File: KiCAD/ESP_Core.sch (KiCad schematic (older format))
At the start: 8 parts, among them J201 Conn_02x04_Counter_Clockwise, U201 ESP32-PICO-D4

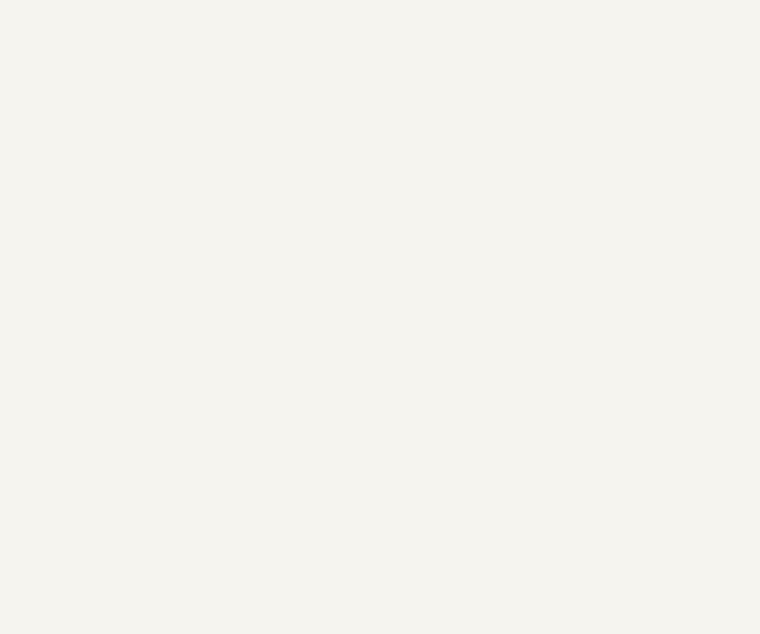
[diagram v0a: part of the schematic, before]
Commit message: Continue work on Schematics
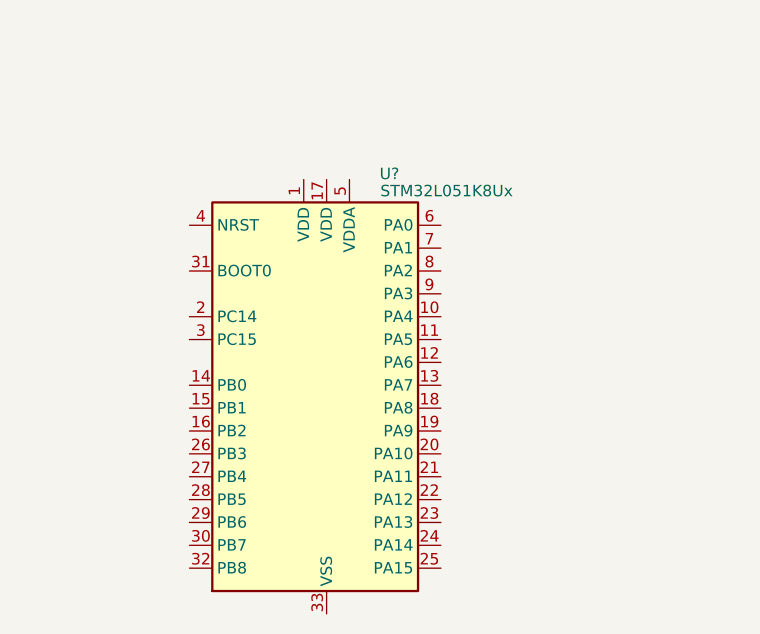
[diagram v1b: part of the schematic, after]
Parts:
- added U?: STM32L051K8Ux, Package_DFN_QFN:QFN-32-1EP_5x5mm_P0.5mm_EP3.45x3.45mm, symbol MCU_ST_STM32L0:STM32L051K8Ux
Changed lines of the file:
@@
 $Descr A4 11693 8268
 encoding utf-8
-Sheet 2 6
+Sheet 2 7
 Title ""
 Date ""
@@
 Text Label 7625 4225 0    50   ~ 0
 STATE_LED
+$Comp
+L MCU_ST_STM32L0:STM32L051K8Ux U?
+U 1 1 6106CA64
+P 2500 5100
+F 0 "U?" H 2775 6025 50  0000 C CNN
+F 1 "STM32L051K8Ux" H 3025 5950 50  0000 C CNN
+F 2 "Package_DFN_QFN:QFN-32-1EP_5x5mm_P0.5mm_EP3.45x3.45mm" H 2000 4200 50  0001 R CNN
+F 3 "http://www.st.com/st-web-ui/static/active/en/resource/technical/document/datasheet/DM00108219.pdf" H 2500 5100 50  0001 C CNN
+	1    2500 5100
+	1    0    0    -1
+$EndComp
 $EndSCHEMATC

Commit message: Add STM32 base circuit for power control and USB, also a lot of other things
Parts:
- removed U?: STM32L051K8Ux, Package_DFN_QFN:QFN-32-1EP_5x5mm_P0.5mm_EP3.45x3.45mm, symbol MCU_ST_STM32L0:STM32L051K8Ux
- added C204: 1uF 0402, Capacitor_SMD:C_0402_1005Metric, symbol Device:C_Small
- added C205: 0.1uF 0402, Capacitor_SMD:C_0402_1005Metric, symbol Device:C_Small
- added PW201: AP7354-33FS4, XasPrints:X2-DFN1010-4, symbol XasParts:AP7354-33FS4
- added R202: 10k 0402, Resistor_SMD:R_0402_1005Metric, symbol Device:R_Small
- added R203: 0402 100k, Resistor_SMD:R_0402_1005Metric, symbol Device:R_Small
- added R204: 0402 33k, Resistor_SMD:R_0402_1005Metric, symbol Device:R_Small
- added R205: 0402 10k, Resistor_SMD:R_0402_1005Metric, symbol Device:R_Small
- added SW201: SW_Push, Button_Switch_SMD:SW_SPST_B3U-1000P, symbol Switch:SW_Push
- added U202: STM32L052K8Ux, Package_DFN_QFN:QFN-32-1EP_5x5mm_P0.5mm_EP3.45x3.45mm, symbol MCU_ST_STM32L0:STM32L052K8Ux
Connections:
- net BOOT: now also U202.26 (PB3)
- net E>P: now also U202.20 (PA10)
- net GND: now also C204.2, C205.2, PW201.2 (GND), PW201.5 (EP), SW201.2, U202.33 (VSS)
- net P>E: now also R205.1
- net RESET: now also U202.27 (PB4)
- net SCL: now reaches U201.17 (IO14)
- net SCL: now also U202.29 (PB6)
- net SDA: now reaches U201.18 (IO12)
- net SDA: now also U202.30 (PB7)
- net AUDIO_LRCK: now reaches U201.36 (IO23)
- net AUDIO_BCK: now reaches U201.38 (IO19)
- net SPKR_DATA: now reaches U201.39 (IO22)
- net MIC_DATA: now reaches U201.42 (IO21)
- net STM_SWDIO: now reaches J201.4 (Pin_4)
- net STM_SWDIO: now also U202.23 (PA13)
- net STM_SWCLK: now reaches J201.5 (Pin_5)
- net STM_SWCLK: now also U202.24 (PA14)
- net +BATT renamed +5V
- net +5V: now also PW201.3 (EN), PW201.4 (VIN)
- new net: C204.1, C205.1, PW201.1 (OUT), R202.1, U202.17 (VDD), U202.5 (VDDA)
- new net: R203.2, R204.1, U202.7 (PA1)
- new net: R204.2, U202.8 (PA2)
- new net: R202.2, SW201.1, U202.6 (PA0)
- new net: R205.2, U202.19 (PA9)
- new net: U202.1 (VDD), U202.4 (NRST)
- new net BAT_ON: U202.3 (PC15)
- new net GLOW_ON: U202.2 (PC14)
- new net MAIN_PWR_ON: U202.18 (PA8)
- new net RAW_BAT: R203.1
- new net USB_DM: U202.21 (PA11)
- new net USB_DP: U202.22 (PA12)
- no-connect marks 13 -> 11

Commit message: Continue work on TapV2's schematic, almost completing it!
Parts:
- added R206: 10k 0402, Resistor_SMD:R_0402_1005Metric, symbol Device:R_Small
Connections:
- net GND: now also U202.31 (BOOT0)
- net STATE_LED: now also U201.14 (IO25)
- net IR_TX: now reaches U201.34 (IO5)
- net IR_RX: now reaches U201.35 (IO18)
- net STM_RST: now reaches J201.8 (Pin_8)
- net STM_RST: now also U202.4 (NRST), R206.2
- net at C204.1, C205.1, PW201.1 (OUT)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: now also U202.1 (VDD), R206.1
- net CAM_CS: now reaches U202.10 (PA4)
- net CAM_DCLK: now reaches U202.11 (PA5)
- net CAM_PILOT_CLOCK: now reaches U202.12 (PA6)
- net CAM_DATA: now reaches U202.13 (PA7)
- no-connect marks 11 -> 10
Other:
- moved on the sheet: C204, C205, PW201, R202, R203, R204, R205, SW201, U202

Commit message: Finalize PCB schematics
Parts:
- added J202: Conn_01x04_Female, Connector_PinHeader_1.27mm:PinHeader_1x04_P1.27mm_Vertical, symbol Connector:Conn_01x04_Female
- added JP201: SolderJumper_3_Bridged12, Jumper:SolderJumper-3_P1.3mm_Open_RoundedPad1.0x1.5mm, symbol Jumper:SolderJumper_3_Bridged12
- added R207: 36R 0402, Resistor_SMD:R_0402_1005Metric, symbol Device:R_Small
- added R208: 10k 0402, Resistor_SMD:R_0402_1005Metric, symbol Device:R_Small
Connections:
- net +3V3: now also J202.2 (Pin_2)
- net AUDIO_LRCK: now also U201.15 (IO26); no longer U201.36 (IO23)
- net GLOW_ON: now also JP201.2 (C); no longer U202.2 (PC14)
- net GND: now also J202.1 (Pin_1), R208.1
- net IR_RX: now also U201.16 (IO27); no longer U201.35 (IO18)
- net MIC_DATA: now also U201.18 (IO12), R208.2; no longer U201.42 (IO21)
- net SDA: now also U201.42 (IO21); no longer U201.18 (IO12)
- net KNOCK_INT: now reaches U201.12 (IO32)
- net EXT_1: now reaches U201.20 (IO13)
- net EXT_1: now also J202.3 (Pin_3)
- net EXT_2: now reaches U201.21 (IO15)
- net EXT_2: now also J202.4 (Pin_4)
- net ESP_GLOW_ON: now reaches U201.24 (IO4)
- net ESP_GLOW_ON: now also JP201.3 (B)
- net ~VUSB_PRESENT: now reaches U202.14 (PB0)
- net ~CHG: now reaches U202.16 (PB2)
- net STATE_LED: no longer names the net of U201.14 (IO25)
- net STATE_LED: now also R207.2; no longer D201.4 (DIN)
- new net: D201.4 (DIN), R207.1
- new net STM_GLOW: JP201.1 (A), U202.2 (PC14)
- no-connect marks 10 -> 24
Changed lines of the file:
@@
 Wire Wire Line
 	9025 4225 8750 4225
-Wire Wire Line
-	8150 4225 7625 4225
-Text Label 7625 4225 0    50   ~ 0
-STATE_LED
 $Comp
 L XasParts:AP7354-33FS4 PW201
@@
 AUDIO_BCK
 Wire Wire Line
-	6275 2525 6875 2525
+	6275 2525 6675 2525
 Text GLabel 6675 4025 2    50   Input ~ 0
 SPKR_DATA
-Text GLabel 6675 4125 2    50   Input ~ 0
+Text GLabel 6675 4325 2    50   Input ~ 0
 AUDIO_LRCK
+Text GLabel 6675 3325 2    50   Input ~ 0
+MIC_DATA
+Wire Wire Line
+	6675 4025 6275 4025
+Wire Wire Line
+	6675 3825 6275 3825
+Wire Wire Line
+	6675 3925 6275 3925
 Text GLabel 6675 3925 2    50   Input ~ 0
-MIC_DATA
-Wire Wire Line
-	6675 4125 6275 4125
-Wire Wire Line
-	6675 4025 6275 4025
-Wire Wire Line
-	6675 3825 6275 3825
-Wire Wire Line
-	6675 3925 6275 3925
-Text GLabel 6675 3325 2    50   Input ~ 0
 SDA
 Text GLabel 6675 3525 2    50   Input ~ 0
@@
 Wire Wire Line
 	6675 3525 6275 3525
-Wire Wire Line
-	6275 3325 6675 3325
 Wire Wire Line
 	3875 4775 3875 4800
@@
 Wire Wire Line
 	1900 5200 1500 5200
-Text GLabel 1500 5100 0    50   Input ~ 0
+Text GLabel 5300 6775 3    50   Input ~ 0
 GLOW_ON
 Text GLabel 1500 5200 0    50   Input ~ 0
@@
 Text GLabel 6675 3025 2    50   Input ~ 0
 IR_TX
-Wire Wire Line
-	6275 3725 6675 3725
-Text GLabel 6675 3725 2    50   Input ~ 0
+Text GLabel 6675 4425 2    50   Input ~ 0
 IR_RX
 Wire Wire Line
@@
 Wire Wire Line
 	2175 1350 2275 1350
-Wire Wire Line
-	6275 4225 6675 4225
-Text Label 6675 4225 0    50   ~ 0
-STATE_LED
+$Comp
+L Jumper:SolderJumper_3_Bridged12 JP?
+U 1 1 614128B8
+P 5300 6550
+AR Path="/60EE6959/614128B8" Ref="JP?"  Part="1"
+AR Path="/60EDF44C/614128B8" Ref="JP201"  Part="1"
+F 0 "JP201" H 5300 6755 50  0000 C CNN
+F 1 "SolderJumper_3_Bridged12" H 5300 6664 50  0000 C CNN
+F 2 "Jumper:SolderJumper-3_P1.3mm_Open_RoundedPad1.0x1.5mm" H 5300 6550 50  0001 C CNN
+F 3 "~" H 5300 6550 50  0001 C CNN
+	1    5300 6550
+	1    0    0    -1
+$EndComp
+Wire Wire Line
+	5300 6775 5300 6700
+Wire Wire Line
+	5100 6550 4625 6550
+Text Label 4625 6550 0    50   ~ 0
+STM_GLOW
+Text Label 1500 5100 0    50   ~ 0
+STM_GLOW
+Wire Wire Line
+	5500 6550 6225 6550
+Wire Wire Line
+	6275 2925 6950 2925
+Text Label 6950 2925 2    50   ~ 0
+ESP_GLOW_ON
+Text Label 6225 6550 2    50   ~ 0
+ESP_GLOW_ON
+$Comp
+L Connector:Conn_01x04_Female J202
+U 1 1 6145C0CC
+P 8625 2950
+F 0 "J202" H 8652 2926 50  0000 L CNN
+F 1 "Conn_01x04_Female" H 8652 2835 50  0000 L CNN
+F 2 "Connector_PinHeader_1.27mm:PinHeader_1x04_P1.27mm_Vertical" H 8625 2950 50  0001 C CNN
+F 3 "~" H 8625 2950 50  0001 C CNN
+	1    8625 2950
+	1    0    0    -1
+$EndComp
+Wire Wire Line
+	8425 2850 8025 2850
+$Comp
+L power:GND #PWR0161
+U 1 1 6145FA1F
+P 8025 2850
+F 0 "#PWR0161" H 8025 2600 50  0001 C CNN
+F 1 "GND" V 8030 2722 50  0000 R CNN
+F 2 "" H 8025 2850 50  0001 C CNN
+F 3 "" H 8025 2850 50  0001 C CNN
+	1    8025 2850
+	0    1    1    0
+$EndComp
+$Comp
+L power:+3.3V #PWR0162
+U 1 1 6145FABB
+P 8025 2950
+F 0 "#PWR0162" H 8025 2800 50  0001 C CNN
+F 1 "+3.3V" V 8040 3078 50  0000 L CNN
+F 2 "" H 8025 2950 50  0001 C CNN
+F 3 "" H 8025 2950 50  0001 C CNN
+	1    8025 2950
+	0    -1   -1   0
+$EndComp
+Wire Wire Line
+	8025 2950 8425 2950
+Wire Wire Line
+	8425 3050 8025 3050
+Text Label 8025 3050 0    50   ~ 0
+EXT_1
+Text Label 8025 3150 0    50   ~ 0
+EXT_2
+Wire Wire Line
+	8025 3150 8425 3150
+Text Label 6675 3450 0    50   ~ 0
+EXT_1
+Wire Wire Line
+	6675 3450 6400 3450
+Wire Wire Line
+	6400 3450 6400 3425
+Wire Wire Line
+	6400 3425 6275 3425
+Wire Wire Line
+	6275 3625 6400 3625
+Wire Wire Line
+	6400 3625 6400 3650
+Wire Wire Line
+	6400 3650 6675 3650
+Text Label 6675 3650 0    50   ~ 0
+EXT_2
+Text GLabel 1775 5400 0    50   Input ~ 0
+~VUSB_PRESENT
+Wire Wire Line
+	1775 5400 1900 5400
+Text GLabel 1775 5525 0    50   Input ~ 0
+~CHG
+Wire Wire Line
+	1775 5525 1825 5525
+Wire Wire Line
+	1825 5525 1825 5600
+Wire Wire Line
+	1825 5600 1900 5600
+NoConn ~ 1900 5500
+NoConn ~ 1900 5900
+NoConn ~ 1900 6200
+NoConn ~ 3000 6200
+NoConn ~ 3000 5000
+NoConn ~ 6275 3125
+NoConn ~ 6275 3225
+NoConn ~ 6275 2725
+NoConn ~ 6275 4625
+NoConn ~ 6275 4725
+NoConn ~ 6275 4825
+NoConn ~ 6275 5025
+Text GLabel 6675 4525 2    50   Input ~ 0
+KNOCK_INT
+Wire Wire Line
+	6275 4525 6675 4525
+$Comp
+L Device:R_Small R207
+U 1 1 61456881
+P 7350 4225
+F 0 "R207" H 7409 4271 50  0000 L CNN
+F 1 "36R 0402" H 7409 4180 50  0000 L CNN
+F 2 "Resistor_SMD:R_0402_1005Metric" H 7350 4225 50  0001 C CNN
+F 3 "~" H 7350 4225 50  0001 C CNN
+	1    7350 4225
+	0    1    1    0
+$EndComp
+Wire Wire Line
+	7450 4225 8150 4225
+Wire Wire Line
+	6275 4225 7250 4225
+NoConn ~ 6275 3725
+NoConn ~ 6275 4125
+Wire Wire Line
+	6275 4425 6675 4425
+Wire Wire Line
+	6275 4325 6675 4325
+Wire Wire Line
+	6675 3325 6550 3325
+Wire Wire Line
+	6550 3325 6550 3200
+Connection ~ 6550 3325
+Wire Wire Line
+	6550 3325 6275 3325
+$Comp
+L Device:R_Small R208
+U 1 1 61485685
+P 7225 3200
+F 0 "R208" H 7284 3246 50  0000 L CNN
+F 1 "10k 0402" H 7284 3155 50  0000 L CNN
+F 2 "Resistor_SMD:R_0402_1005Metric" H 7225 3200 50  0001 C CNN
+F 3 "~" H 7225 3200 50  0001 C CNN
+	1    7225 3200
+	0    1    1    0
+$EndComp
+Wire Wire Line
+	6550 3200 7125 3200
+$Comp
+L power:GND #PWR0166
+U 1 1 6148A0BC
+P 7425 3200
+F 0 "#PWR0166" H 7425 2950 50  0001 C CNN
+F 1 "GND" H 7430 3027 50  0000 C CNN
+F 2 "" H 7425 3200 50  0001 C CNN
+F 3 "" H 7425 3200 50  0001 C CNN
+	1    7425 3200
+	0    -1   -1   0
+$EndComp
+Wire Wire Line
+	7425 3200 7325 3200
 $EndSCHEMATC
